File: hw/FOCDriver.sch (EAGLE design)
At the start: 118 parts, among them Q1 BC817, Q2 BC817, Q3 BC817, Q4 BC817, Q5 BC817, Q6 BC817, U1 SN74LVC2G17, U10 LMV321SQ3T2G, U11 LMV321SQ3T2G, U2 AO4606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

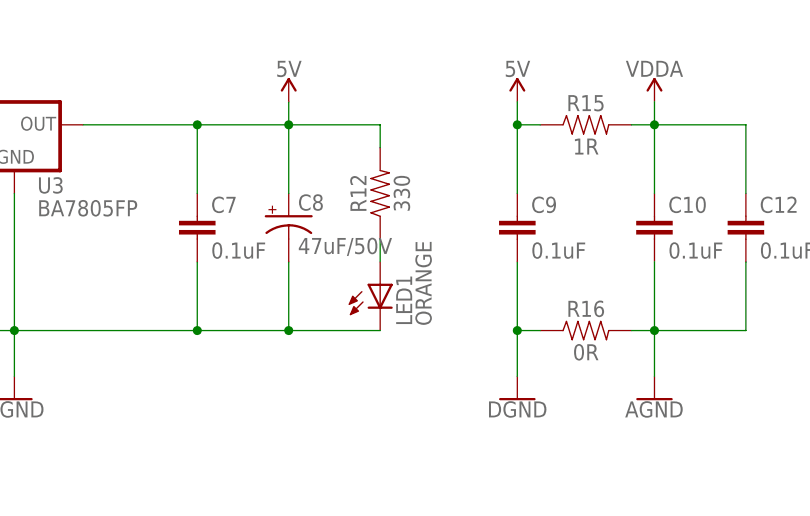
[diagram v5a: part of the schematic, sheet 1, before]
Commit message: refine top silk
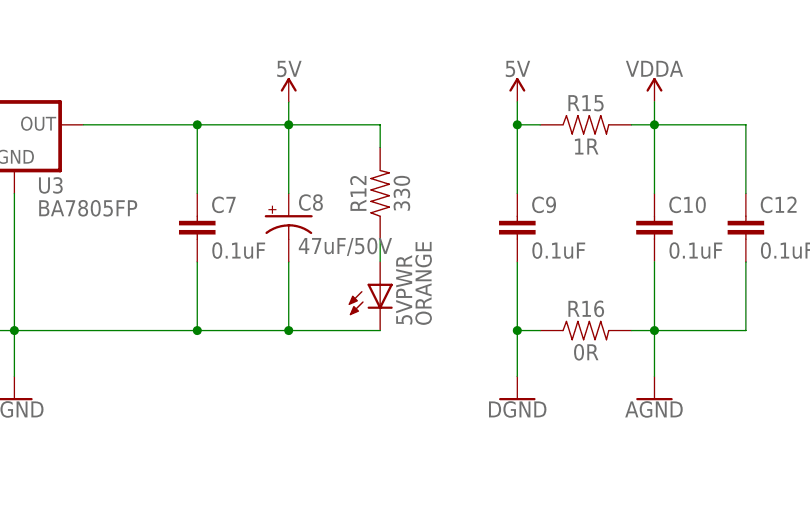
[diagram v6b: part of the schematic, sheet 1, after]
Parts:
- renumbered LED1 to 5VPWR
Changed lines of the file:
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@@
 <part name="FRAME1" library="frames" deviceset="A4L-LOC" device=""/>
 <part name="FRAME2" library="frames" deviceset="A4L-LOC" device=""/>
-<part name="LED1" library="led" deviceset="LED" device="SML0805" value="ORANGE"/>
+<part name="5VPWR" library="led" deviceset="LED" device="SML0805" value="ORANGE"/>
 <part name="R1" library="SparkFun-Resistors" deviceset="RESISTOR" device="0805" value="1K"/>
 <part name="R3" library="SparkFun-Resistors" deviceset="RESISTOR" device="0805" value="1K"/>
@@
 <instance part="U3" gate="G$1" x="78.74" y="66.04"/>
 <instance part="F1" gate="G$1" x="30.48" y="66.04"/>
-<instance part="LED1" gate="G$1" x="119.38" y="48.26"/>
+<instance part="5VPWR" gate="G$1" x="119.38" y="48.26"/>
 <instance part="R12" gate="G$1" x="119.38" y="58.42" rot="R90"/>
 <instance part="R15" gate="G$1" x="142.24" y="66.04"/>
@@
 </segment>
 <segment>
-<pinref part="LED1" gate="G$1" pin="C"/>
+<pinref part="5VPWR" gate="G$1" pin="C"/>
 <pinref part="C8" gate="G$1" pin="-"/>
 <wire x1="78.74" y1="43.18" x2="78.74" y2="58.42" width="0.1524" layer="91"/>
@@
 <net name="N$31" class="0">
 <segment>
-<pinref part="LED1" gate="G$1" pin="A"/>
+<pinref part="5VPWR" gate="G$1" pin="A"/>
 <wire x1="119.38" y1="50.8" x2="119.38" y2="53.34" width="0.1524" layer="91"/>
 <pinref part="R12" gate="G$1" pin="1"/>

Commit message: fix error
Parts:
- removed C28: 0.1uF, SparkFun-Capacitors:1.0UF-0805-25V-10%
- added C29: 0.1u, rcl:C-EUC0805
- added J11: (no value), SparkFun-Connectors:CONN_02
- C1, C10, C12, C13, C6, C7, C9: value 0.1uF -> 100n; device SparkFun-Capacitors:1.0UF-0805-25V-10% -> rcl:C-EUC0805
- C15, C16, C17, C21, C22, C23: value 56pF -> 56p; device SparkFun-Capacitors:1.0UF-0805-25V-10% -> rcl:C-EUC0805
- C18, C19, C2, C20, C27, C4: value 0.1uF -> 0.1u; device SparkFun-Capacitors:1.0UF-0805-25V-10% -> rcl:C-EUC0805
- C24, C25, C26: value 1nF -> 1n; device SparkFun-Capacitors:1.0UF-0805-25V-10% -> rcl:C-EUC0805
- Q1, Q2, Q3, Q4, Q5, Q6: device SparkFun-DiscreteSemi:TRANS_NPN-MMBT2222AL -> transistor-npn:BC817-40SMD
- R1, R10, R11, R12, R13, R17, R18, R19, R2, R20, R21, R23, R3, R4, R46, R49, R5, R50, R51, R52, R53, R8, R9: device SparkFun-Resistors:RESISTOR0805 -> rcl:R-US_R0805
- R15: value 1R -> 0; device SparkFun-Resistors:RESISTOR0805 -> rcl:R-US_R0805
- R16, R6: value 0R -> 0; device SparkFun-Resistors:RESISTOR0805 -> rcl:R-US_R0805
- R25, R26, R27, R28, R29, R30, R31, R32, R33, R34, R35, R36, R43, R44, R45: value 1K 1% -> 1K; device SparkFun-Resistors:RESISTOR0805 -> rcl:R-US_R0805
- R37, R38, R39, R40, R41, R42, R47, R48: value 20K 1% -> 20K; device SparkFun-Resistors:RESISTOR0805 -> rcl:R-US_R0805
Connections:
- net 5V: now also C1.2, C13.2, C6.2, J11.2, R23.1; no longer C1.1, C13.1, C6.1, R23.2
- net AGND: now also C29.2; no longer C28.2
- net DGND: now also C1.1, C13.1, C6.1, J11.1; no longer C1.2, C13.2, C6.2
- net N$15: now also C21.1; no longer C21.2
- net N$20: now also C22.1; no longer C22.2
- net N$25: now also C23.1; no longer C23.2
- net N$4: now also R23.2; no longer R23.1
- net VDDA: now also C29.1; no longer C28.1
- net VREF: now also C21.2, C22.2, C23.2; no longer C21.1, C22.1, C23.1
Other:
- moved on the sheet: C1, C13, C21, C22, C23, C4, C6, R23, R40, R41, R42

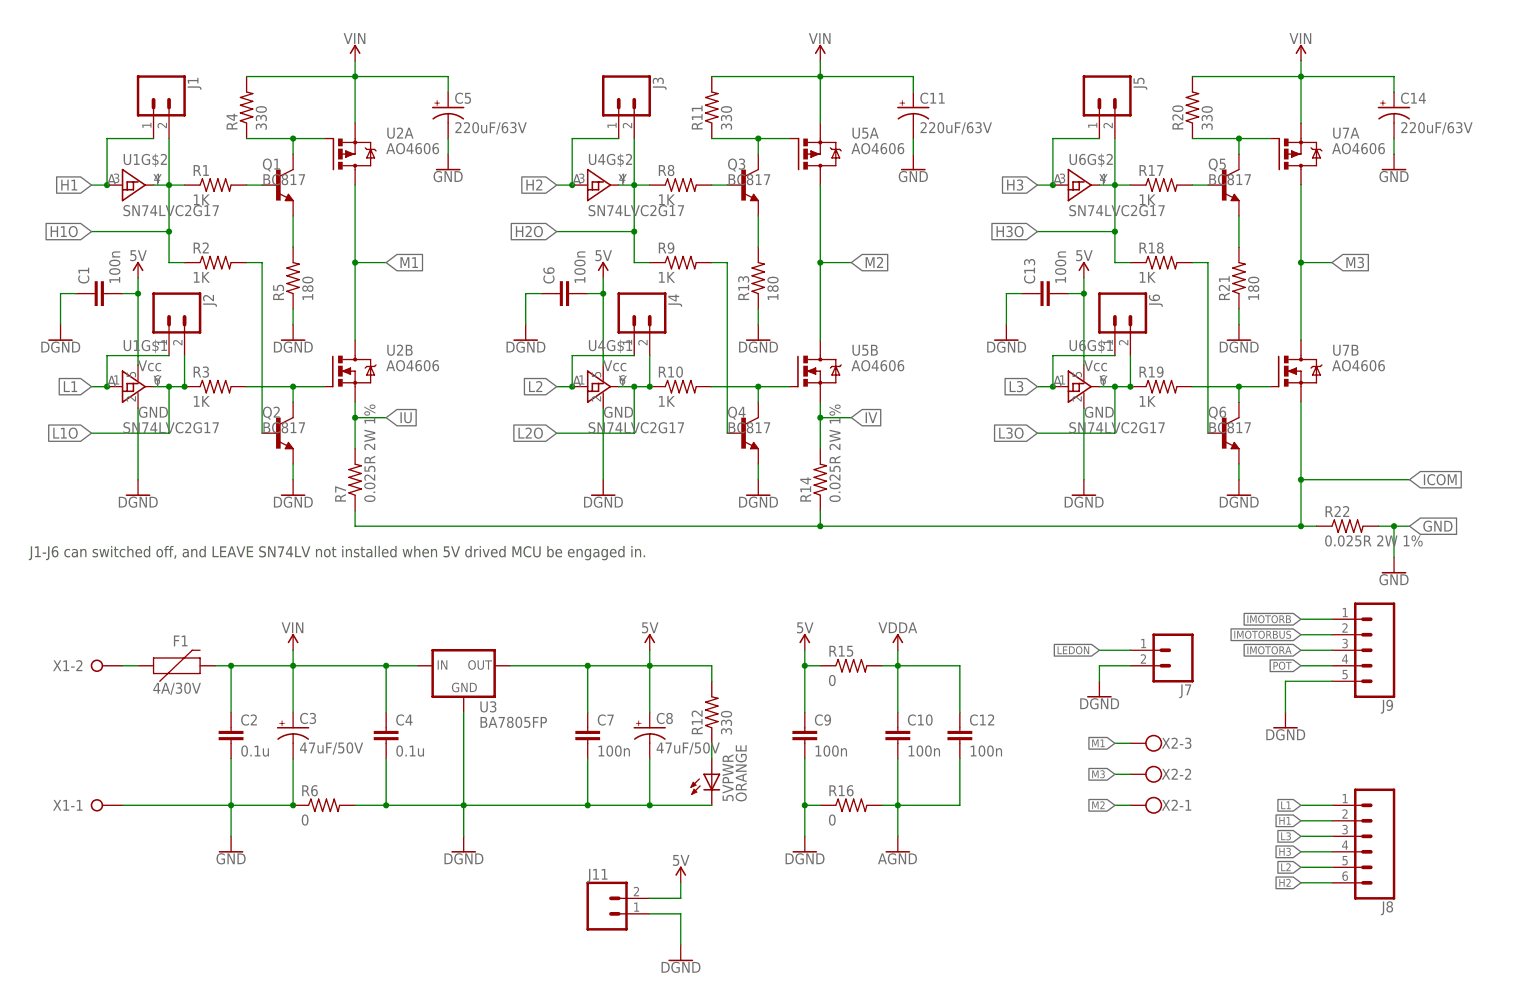
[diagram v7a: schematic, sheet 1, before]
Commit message: fix layout bugs
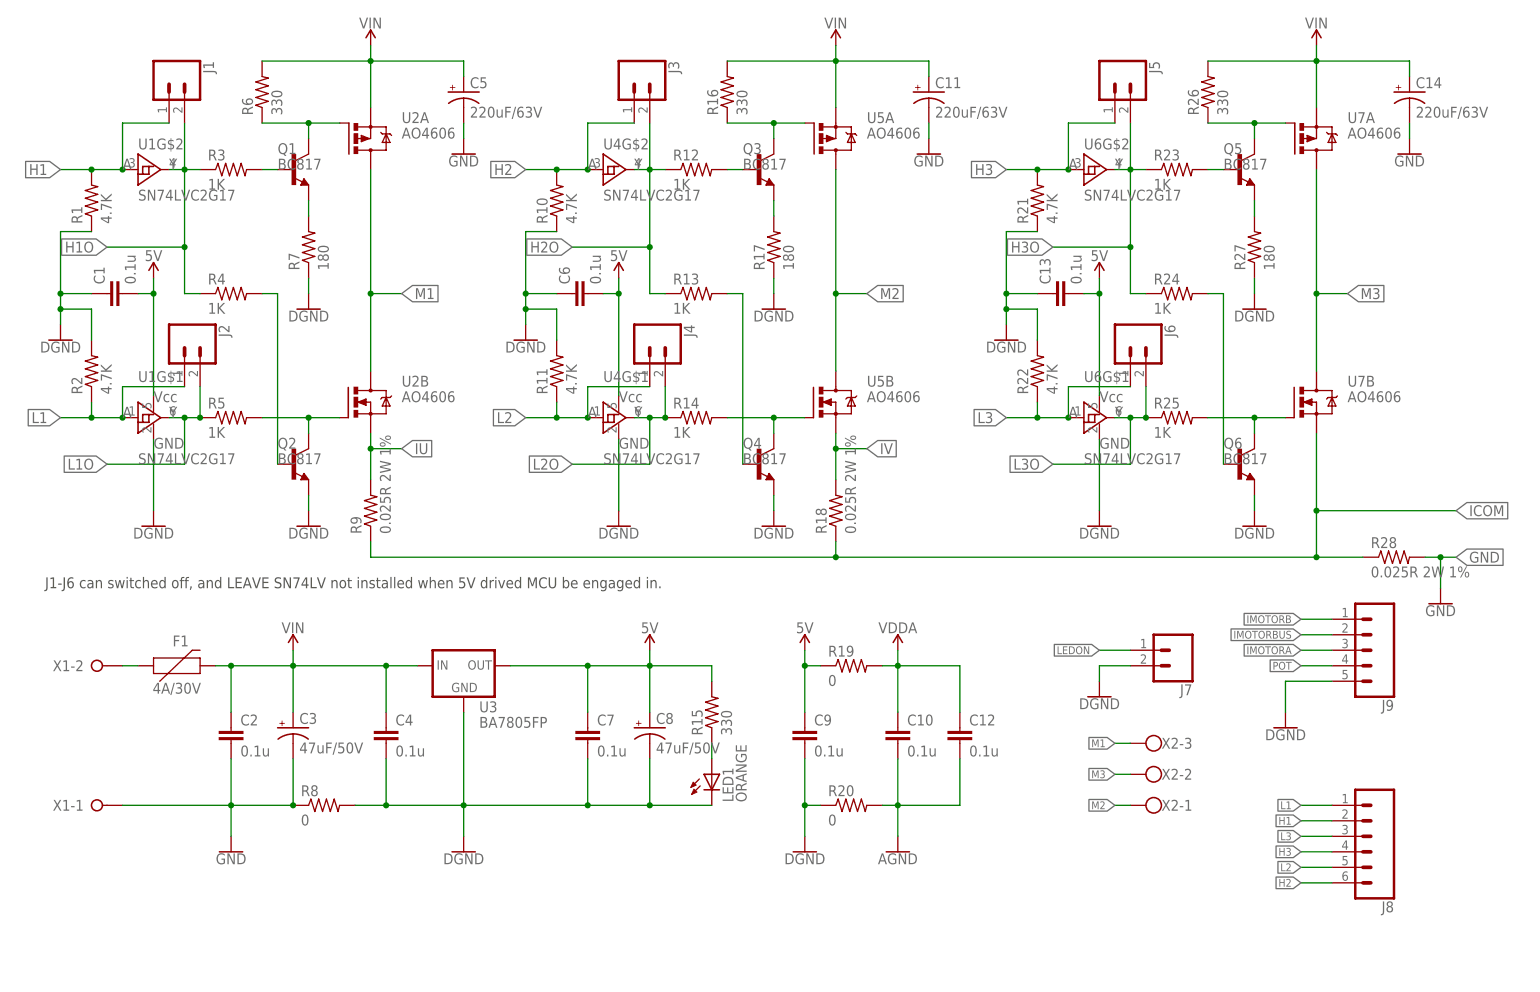
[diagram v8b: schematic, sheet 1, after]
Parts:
- added J12, J13: (no value), SparkFun-Connectors:CONN_01PTH_NO_SILK_YES_STOP
- added J14: (no value), SparkFun-Connectors:CONN_04
- added R54: 20K, rcl:R-US_R0805
- added R55, R56, R57, R58, R59: 330, rcl:R-US_R0805
- C1, C10, C12, C13, C6, C7, C9: value 100n -> 0.1u
- J10: device SparkFun-Connectors:CONN_04 -> SparkFun-Connectors:CONN_01PTH_NO_SILK_YES_STOP
- J11: device SparkFun-Connectors:CONN_02 -> SparkFun-Connectors:CONN_01PTH_NO_SILK_YES_STOP
- R1, R10, R2: value 1K -> 4.7K
- R11: value 330 -> 4.7K
- R12, R4, R49, R50, R51: value 330 -> 1K
- R13, R5: value 180 -> 1K
- R14: value 0.025R 2W 1% -> 1K; device resistor:R-US_R2512 -> rcl:R-US_R0805
- R15, R16, R6: value 0 -> 330
- R17, R27: value 1K -> 180
- R18, R28, R9: value 1K -> 0.025R 2W 1%; device rcl:R-US_R0805 -> resistor:R-US_R2512
- R19, R8: value 1K -> 0
- R20: value 330 -> 0
- R21: value 180 -> 4.7K
- R22: value 0.025R 2W 1% -> 4.7K; device resistor:R-US_R2512 -> rcl:R-US_R0805
- R23: value 5.6K -> 1K
- R24: value 10K -> 1K; device pot:TRIM_US-CT6 -> rcl:R-US_R0805
- R26: value 1K -> 330
- R29: value 1K -> 5.6K
- R30: value 1K -> 10K; device rcl:R-US_R0805 -> pot:TRIM_US-CT6
- R37, R38, R39, R40, R41, R42: value 20K -> 1K
- R43, R44, R45: value 1K -> 20K
- R46, R53: value 330 -> 20K
- R7: value 0.025R 2W 1% -> 180; device resistor:R-US_R2512 -> rcl:R-US_R0805
- U10, U11, U8, U9: value LMV321SQ3T2G -> LMV321IDBVRG4; device LMV321SQ3T2G:LMV321SQ3T2G -> LMV321IDBVRG4:LMV321IDBVRG4
- renumbered 5VPWR to LED1, C29 to C28
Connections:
- net 3V3FROMMCU: now also J14.1, J14.2; no longer J10.1, J10.2
- net 5V: now also J10.1, J12.1, R15.2, R19.1, R29.1; no longer J11.2, R12.2, R15.1, R23.1
- net AGND: now also R20.2, R54.1; no longer R16.2, R48.1
- net DGND: now also J13.1, R1.1, R10.1, R11.2, R17.1, R2.2, R20.1, R22.2, R27.1, R30.A, R7.1, R8.2; no longer R13.1, R16.1, R24.A, R5.1, R6.2
- net GND: now also R28.2, R35.1, R8.1; no longer R22.2, R29.1, R6.1
- net H1: now also R1.2
- net H1O: now also R3.1, R4.1, R52.2; no longer R1.1, R2.1, R46.2
- net H2: now also R10.2
- net H2O: now also R12.1, R13.1, R56.2; no longer R50.2, R8.1, R9.1
- net H3: now also R21.2
- net H3O: now also R23.1, R24.1, R58.2; no longer R17.1, R18.1, R52.2
- net ICOM: now also R18.1, R28.1, R31.1, R33.1, R36.1, R9.1; no longer R14.1, R22.1, R25.1, R27.1, R30.1, R7.1
- net IMOTORA: now also R49.2; no longer R43.2
- net IMOTORB: now also R50.2; no longer R44.2
- net IMOTORBUS: now also R51.2; no longer R45.2
- net IU: now also R32.1, R9.2; no longer R26.1, R7.2
- net IV: now also R18.2, R34.1; no longer R14.2, R28.1
- net L1: now also R2.1
- net L1O: now also R5.1, R55.2; no longer R3.1, R49.2
- net L2: now also R11.1
- net L2O: now also R14.1, R57.2; no longer R10.1, R51.2
- net L3: now also R22.1
- net L3O: now also R25.1, R59.2; no longer R19.1, R53.2
- net N$10: now also R6.1; no longer R4.1
- net N$11: now also R31.2, R37.1; no longer R25.2, R31.1
- net N$12: now also R32.2, R38.1; no longer R26.2, R32.1
- net N$13: now also R37.2, R43.1; no longer R31.2, R37.1
- net N$14: now also R33.2, R39.1; no longer R27.2, R33.1
- net N$15: now also R38.2, R46.1; no longer R32.2, R40.1
- net N$16: now also R43.2, R49.1; no longer R37.2, R43.1
- net N$17: now also R34.2, R40.1; no longer R28.2, R34.1
- net N$18: now also R53.1, R54.2; no longer R47.1, R48.2
- net N$19: now also R39.2, R44.1; no longer R33.2, R38.1
- net N$20: now also R40.2, R47.1; no longer R34.2, R41.1
- net N$21: now also R44.2, R50.1; no longer R38.2, R44.1
- net N$22: now also R35.2, R41.1; no longer R29.2, R35.1
- net N$23: now also R36.2, R42.1; no longer R30.2, R36.1
- net N$24: now also R41.2, R45.1; no longer R35.2, R39.1
- net N$25: now also R42.2, R48.1; no longer R36.2, R42.1
- net N$26: now also R45.2, R51.1; no longer R39.2, R45.1
- net N$28: now also R27.2; no longer R21.2
- net N$3: now also R25.2; no longer R19.2
- net N$30: now also R3.2; no longer R1.2
- net N$31: now also R15.1; no longer R12.1
- net N$32: now also R4.2; no longer R2.2
- net N$33: now also R52.1; no longer R46.1
- net N$34: now also R55.1; no longer R49.1
- net N$35: now also R56.1; no longer R50.1
- net N$36: now also R57.1; no longer R51.1
- net N$37: now also R58.1; no longer R52.1
- net N$38: now also R59.1; no longer R53.1
- net N$39: now also R12.2; no longer R8.2
- net N$4: now also R29.2, R30.E; no longer R23.2, R24.E
- net N$40: now also R7.2; no longer R5.2
- net N$41: now also R13.2; no longer R9.2
- net N$42: now also R23.2; no longer R17.2
- net N$43: now also R17.2; no longer R13.2
- net N$44: now also R24.2; no longer R18.2
- net N$6: now also R26.1; no longer R20.1
- net N$7: now also R14.2; no longer R10.2
- net N$8: now also R16.1; no longer R11.1
- net N$9: now also R5.2; no longer R3.2
- net POT: now also R30.S; no longer R24.S
- net PWRDIV: now also J14.3, R53.2; no longer J10.3, R47.2
- net VDDA: now also J14.4, R19.2; no longer J10.4, R15.2
- net VIN: now also R16.2, R26.2, R6.2; no longer R11.2, R20.2, R4.2
- net VREF: now also R46.2, R47.2, R48.2; no longer R40.2, R41.2, R42.2
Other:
- moved on the sheet: C1, C11, C13, C14, C5, C6, J1, J2, J3, J4, J5, J6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
